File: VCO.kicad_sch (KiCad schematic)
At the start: 69 parts, among them K1 SW_SPST, K1-1 Conn_01x01, K1-2 Conn_01x01, K2 SW_SPST, K2-1 Conn_01x01, K2-2 Conn_01x01, K3 SW_SPST, K3-1 Conn_01x01, K3-2 Conn_01x01, P1-1-3 Conn_01x01, P1-2 Conn_01x01, P2 100k, P2-3 Conn_01x01, P3 100k, P3-1 Conn_01x01, P3-3 Conn_01x01, P4 4k7, P4-2 Conn_01x01, P4-3 Conn_01x01, Q3 BC184, Q4 BC183B, Q5 BF244B, Q6 BC184, Q7 BF244B, Q8 BC184, U1 7413, U2 7490, U4 UA747

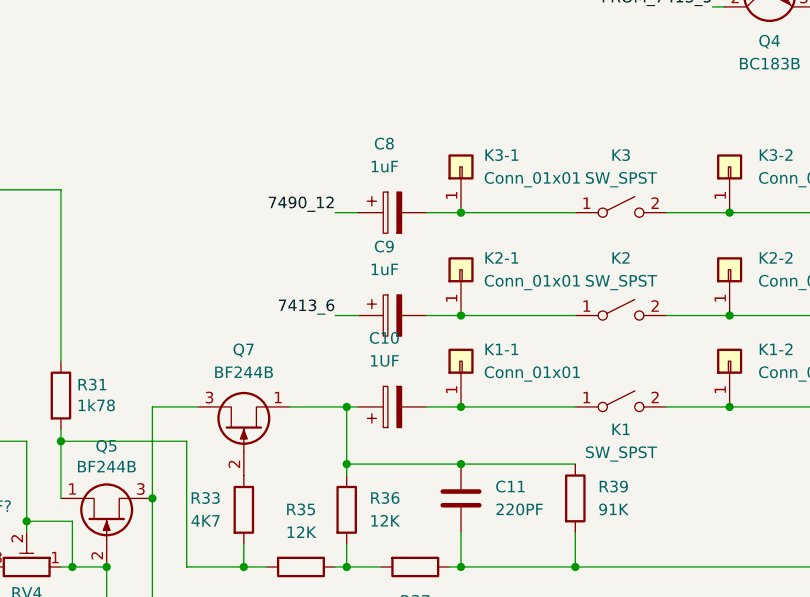
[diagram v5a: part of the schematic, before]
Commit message: Label connectors, update footprints
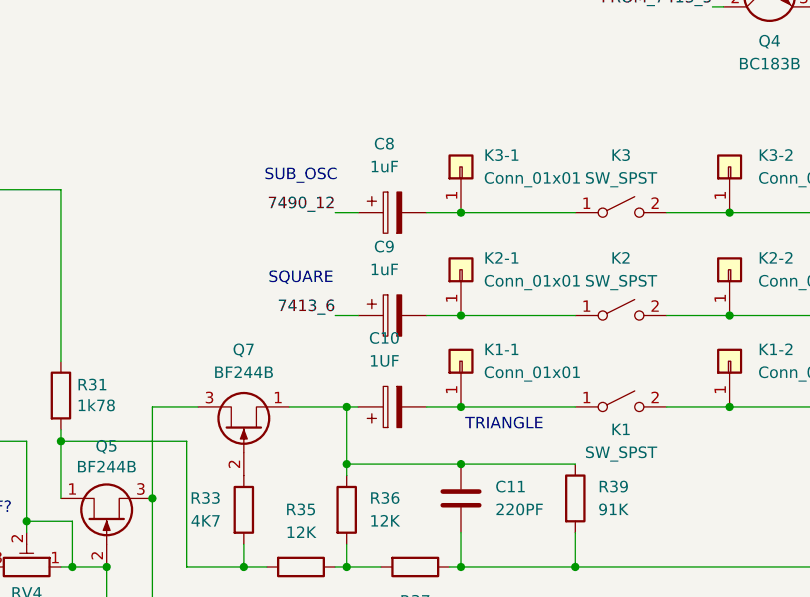
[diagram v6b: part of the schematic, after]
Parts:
- C10, C8: footprint (none) -> Capacitor_THT:CP_Radial_D6.3mm_P2.50mm
- C11, C6, C7: footprint (none) -> Capacitor_THT:C_Disc_D5.0mm_W2.5mm_P5.00mm
- C9: footprint (none) -> Capacitor_THT:CP_Radial_D8.0mm_P5.00mm
- D1, D2: footprint (none) -> Diode_THT:D_A-405_P10.16mm_Horizontal
- K1-1, K1-2, K2-1, K2-2, K3-1, K3-2, P1-1-3, P1-2, P2-3, P3-1, P3-3, P4-2, P4-3: footprint (none) -> Connector_PinHeader_2.54mm:PinHeader_1x01_P2.54mm_Vertical
- R18, R19, R20, R21, R23, R24, R25, R26, R27, R28, R29, R30, R31, R32, R33, R34, R35, R36, R37, R38, R39, R40, R41, R42, R43, R44, R45: footprint (none) -> Resistor_THT:R_Axial_DIN0207_L6.3mm_D2.5mm_P15.24mm_Horizontal
- RV16, RV17, RV22, RV4, RV46: footprint (none) -> Potentiometer_THT:Potentiometer_Bourns_3296W_Vertical
- U1, U2, U4: footprint (none) -> Package_DIP:DIP-14_W7.62mm_Socket_LongPads
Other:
- note added: "SQUARE"
- note added: "SUB_OSC"
- note added: "TRIANGLE"
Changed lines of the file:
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@@
 	(generator_version "9.0")
 	(paper "A4")
+	(text "SUB_OSC"
+		(exclude_from_sim no)
+		(at 184.15 58.166 0)
+		(effects
+			(font
+				(size 1.27 1.27)
+			)
+		)
+	)
+	(text "SQUARE"
+		(exclude_from_sim no)
+		(at 184.15 69.596 0)
+		(effects
+			(font
+				(size 1.27 1.27)
+			)
+		)
+	)
+	(text "TRIANGLE"
+		(exclude_from_sim no)
+		(at 206.756 85.852 0)
+		(effects
+			(font
+				(size 1.27 1.27)
+			)
+		)
+	)
 	(text "WTF?"
 		(exclude_from_sim no)
@@
 			)
 		)
-		(property "Footprint" ""
+		(property "Footprint" "Potentiometer_THT:Potentiometer_Bourns_3296W_Vertical"
 			(at 214.63 26.67 0)
 			(effects
@@
 			)
 		)
-		(property "Footprint" ""
+		(property "Footprint" "Resistor_THT:R_Axial_DIN0207_L6.3mm_D2.5mm_P15.24mm_Horizontal"
 			(at 229.87 28.702 90)
 			(effects
@@
 			)
 		)
-		(property "Footprint" ""
+		(property "Footprint" "Resistor_THT:R_Axial_DIN0207_L6.3mm_D2.5mm_P15.24mm_Horizontal"
 			(at 246.38 24.892 90)
 			(effects
@@
 			)
 		)
-		(property "Footprint" ""
+		(property "Footprint" "Package_DIP:DIP-14_W7.62mm_Socket_LongPads"
 			(at 58.42 115.57 0)
 			(effects
@@
 			)
 		)
-		(property "Footprint" ""
+		(property "Footprint" "Resistor_THT:R_Axial_DIN0207_L6.3mm_D2.5mm_P15.24mm_Horizontal"
 			(at 18.542 107.95 90)
 			(effects
@@
 			)
 		)
-		(property "Footprint" ""
+		(property "Footprint" "Resistor_THT:R_Axial_DIN0207_L6.3mm_D2.5mm_P15.24mm_Horizontal"
 			(at 22.098 162.56 90)
 			(effects
@@
 			)
 		)
-		(property "Footprint" ""
+		(property "Footprint" "Package_DIP:DIP-14_W7.62mm_Socket_LongPads"
 			(at 58.42 72.39 0)
 			(effects
@@
 			)
 		)
-		(property "Footprint" ""
+		(property "Footprint" "Capacitor_THT:CP_Radial_D6.3mm_P2.50mm"
 			(at 198.12 63.1952 0)
 			(effects
@@
 			)
 		)
-		(property "Footprint" ""
+		(property "Footprint" "Resistor_THT:R_Axial_DIN0207_L6.3mm_D2.5mm_P15.24mm_Horizontal"
 			(at 248.92 60.452 90)
 			(effects
@@
 			)
 		)
-		(property "Footprint" ""
+		(property "Footprint" "Resistor_THT:R_Axial_DIN0207_L6.3mm_D2.5mm_P15.24mm_Horizontal"
 			(at 248.92 71.882 90)
 			(effects
@@
 			)
 		)
-		(property "Footprint" ""
+		(property "Footprint" "Resistor_THT:R_Axial_DIN0207_L6.3mm_D2.5mm_P15.24mm_Horizontal"
 			(at 248.92 82.042 90)
 			(effects
@@
 			)
 		)
-		(property "Footprint" ""
+		(property "Footprint" "Resistor_THT:R_Axial_DIN0207_L6.3mm_D2.5mm_P15.24mm_Horizontal"
 			(at 141.732 76.2 90)
 			(effects
@@
 			)
 		)
-		(property "Footprint" ""
+		(property "Footprint" "Capacitor_THT:C_Disc_D5.0mm_W2.5mm_P5.00mm"
 			(at 127.3048 90.805 0)
 			(effects
@@
 			)
 		)
-		(property "Footprint" ""
+		(property "Footprint" "Potentiometer_THT:Potentiometer_Bourns_3296W_Vertical"
 			(at 153.67 101.6 0)
 			(effects
@@
 			)
 		)
-		(property "Footprint" ""
+		(property "Footprint" "Potentiometer_THT:Potentiometer_Bourns_3296W_Vertical"
 			(at 120.65 63.5 0)
 			(effects
@@
 			)
 		)
-		(property "Footprint" ""
+		(property "Footprint" "Diode_THT:D_A-405_P10.16mm_Horizontal"
 			(at 128.27 64.77 0)
 			(effects
@@
 			)
 		)
-		(property "Footprint" ""
+		(property "Footprint" "Diode_THT:D_A-405_P10.16mm_Horizontal"
 			(at 128.27 53.34 0)
 			(effects
@@
 			)
 		)
-		(property "Footprint" ""
+		(property "Footprint" "Resistor_THT:R_Axial_DIN0207_L6.3mm_D2.5mm_P15.24mm_Horizontal"
 			(at 155.702 82.55 90)
 			(effects
@@
 			)
 		)
-		(property "Footprint" ""
+		(property "Footprint" "Capacitor_THT:CP_Radial_D8.0mm_P5.00mm"
 			(at 198.12 74.6252 0)
 			(effects
@@
 			)
 		)
-		(property "Footprint" ""
+		(property "Footprint" "Capacitor_THT:CP_Radial_D6.3mm_P2.50mm"
 			(at 198.12 82.8548 0)
 			(effects
@@
 			)
 		)
-		(property "Footprint" ""
+		(property "Footprint" "Resistor_THT:R_Axial_DIN0207_L6.3mm_D2.5mm_P15.24mm_Horizontal"
 			(at 176.022 95.25 90)
 			(effects
@@
 			)
 		)
-		(property "Footprint" ""
+		(property "Footprint" "Resistor_THT:R_Axial_DIN0207_L6.3mm_D2.5mm_P15.24mm_Horizontal"
 			(at 184.15 99.822 90)
 			(effects
@@
 			)
 		)
-		(property "Footprint" ""
+		(property "Footprint" "Resistor_THT:R_Axial_DIN0207_L6.3mm_D2.5mm_P15.24mm_Horizontal"
 			(at 196.85 99.822 90)
 			(effects
@@
 			)
 		)
-		(property "Footprint" ""
+		(property "Footprint" "Resistor_THT:R_Axial_DIN0207_L6.3mm_D2.5mm_P15.24mm_Horizontal"
 			(at 187.452 95.25 90)
 			(effects
@@
 			)
 		)
-		(property "Footprint" ""
+		(property "Footprint" "Capacitor_THT:C_Disc_D5.0mm_W2.5mm_P5.00mm"
 			(at 202.8952 97.79 0)
 			(effects
@@
 			)
 		)
-		(property "Footprint" ""
+		(property "Footprint" "Resistor_THT:R_Axial_DIN0207_L6.3mm_D2.5mm_P15.24mm_Horizontal"
 			(at 212.852 93.98 90)
 			(effects
@@
 			)
 		)
-		(property "Footprint" ""
+		(property "Footprint" "Resistor_THT:R_Axial_DIN0207_L6.3mm_D2.5mm_P15.24mm_Horizontal"
 			(at 116.84 123.952 90)
 			(effects
@@
 			)
 		)
-		(property "Footprint" ""
+		(property "Footprint" "Potentiometer_THT:Potentiometer_Bourns_3296W_Vertical"
 			(at 106.68 152.4 0)
 			(effects
@@
 			)
 		)
-		(property "Footprint" ""
+		(property "Footprint" "Resistor_THT:R_Axial_DIN0207_L6.3mm_D2.5mm_P15.24mm_Horizontal"
 			(at 116.84 150.622 90)
 			(effects
@@
 			)
 		)
-		(property "Footprint" ""
+		(property "Footprint" "Resistor_THT:R_Axial_DIN0207_L6.3mm_D2.5mm_P15.24mm_Horizontal"
 			(at 137.922 115.57 90)
 			(effects
@@
 			)
 		)
-		(property "Footprint" ""
+		(property "Footprint" "Resistor_THT:R_Axial_DIN0207_L6.3mm_D2.5mm_P15.24mm_Horizontal"
 			(at 128.27 123.952 90)
 			(effects
@@
 			)
 		)
-		(property "Footprint" ""
+		(property "Footprint" "Resistor_THT:R_Axial_DIN0207_L6.3mm_D2.5mm_P15.24mm_Horizontal"
 			(at 146.812 125.73 90)
 			(effects
@@
 			)
 		)
-		(property "Footprint" ""
+		(property "Footprint" "Resistor_THT:R_Axial_DIN0207_L6.3mm_D2.5mm_P15.24mm_Horizontal"
 			(at 168.402 113.665 90)
 			(effects
@@
 			)
 		)
-		(property "Footprint" ""
+		(property "Footprint" "Package_DIP:DIP-14_W7.62mm_Socket_LongPads"
 			(at 162.56 146.05 0)
 			(effects
@@
 			)
 		)
-		(property "Footprint" ""
+		(property "Footprint" "Package_DIP:DIP-14_W7.62mm_Socket_LongPads"
 			(at 217.17 148.59 0)
 			(effects
@@
 			)
 		)
-		(property "Footprint" ""
+		(property "Footprint" "Capacitor_THT:C_Disc_D5.0mm_W2.5mm_P5.00mm"
 			(at 161.29 159.7152 0)
 			(effects
@@
 			)
 		)
-		(property "Footprint" ""
+		(property "Footprint" "Resistor_THT:R_Axial_DIN0207_L6.3mm_D2.5mm_P15.24mm_Horizontal"
 			(at 176.022 143.51 90)
 			(effects
@@
 			)
 		)
-		(property "Footprint" ""
+		(property "Footprint" "Resistor_THT:R_Axial_DIN0207_L6.3mm_D2.5mm_P15.24mm_Horizontal"
 			(at 215.9 159.512 90)
 			(effects
@@
 			)
 		)
-		(property "Footprint" ""
+		(property "Footprint" "Resistor_THT:R_Axial_DIN0207_L6.3mm_D2.5mm_P15.24mm_Horizontal"
 			(at 203.962 142.24 90)
 			(effects
@@
 			)
 		)
-		(property "Footprint" ""
+		(property "Footprint" "Resistor_THT:R_Axial_DIN0207_L6.3mm_D2.5mm_P15.24mm_Horizontal"
 			(at 152.908 140.97 90)
 			(effects
@@
 			)
 		)
-		(property "Footprint" ""
+		(property "Footprint" "Resistor_THT:R_Axial_DIN0207_L6.3mm_D2.5mm_P15.24mm_Horizontal"
 			(at 200.66 150.622 90)
 			(effects
@@
 			)
 		)
-		(property "Footprint" ""
+		(property "Footprint" "Resistor_THT:R_Axial_DIN0207_L6.3mm_D2.5mm_P15.24mm_Horizontal"
 			(at 239.268 140.97 90)
 			(effects
@@
 			)
 		)
-		(property "Footprint" ""
+		(property "Footprint" "Potentiometer_THT:Potentiometer_Bourns_3296W_Vertical"
 			(at 237.49 148.59 0)
 			(effects
@@
 			)
 		)
-		(property "Footprint" ""
+		(property "Footprint" "Resistor_THT:R_Axial_DIN0207_L6.3mm_D2.5mm_P15.24mm_Horizontal"
 			(at 138.43 172.212 90)
 			(effects
@@
 			)
 		)
-		(property "Footprint" ""
+		(property "Footprint" "Connector_PinHeader_2.54mm:PinHeader_1x01_P2.54mm_Vertical"
 			(at 111.125 130.81 0)
 			(effects
@@
 			)
 		)
-		(property "Footprint" ""
+		(property "Footprint" "Connector_PinHeader_2.54mm:PinHeader_1x01_P2.54mm_Vertical"
 			(at 201.93 57.15 0)
 			(effects
@@
 			)
 		)
-		(property "Footprint" ""
+		(property "Footprint" "Connector_PinHeader_2.54mm:PinHeader_1x01_P2.54mm_Vertical"
 			(at 201.93 78.74 0)
 			(effects
@@
 			)
 		)
-		(property "Footprint" ""
+		(property "Footprint" "Connector_PinHeader_2.54mm:PinHeader_1x01_P2.54mm_Vertical"
 			(at 231.775 57.15 0)
 			(effects
@@
 			)
 		)
-		(property "Footprint" ""
+		(property "Footprint" "Connector_PinHeader_2.54mm:PinHeader_1x01_P2.54mm_Vertical"
 			(at 231.775 78.74 0)
 			(effects
@@
 			)
 		)
-		(property "Footprint" ""
+		(property "Footprint" "Connector_PinHeader_2.54mm:PinHeader_1x01_P2.54mm_Vertical"
 			(at 134.62 120.65 0)
 			(effects
@@
 			)
 		)
-		(property "Footprint" ""
+		(property "Footprint" "Connector_PinHeader_2.54mm:PinHeader_1x01_P2.54mm_Vertical"
 			(at 201.93 68.58 0)
 			(effects
@@
 			)
 		)
-		(property "Footprint" ""
+		(property "Footprint" "Connector_PinHeader_2.54mm:PinHeader_1x01_P2.54mm_Vertical"
 			(at 231.775 68.58 0)
 			(effects
@@
 			)
 		)
-		(property "Footprint" ""
+		(property "Footprint" "Connector_PinHeader_2.54mm:PinHeader_1x01_P2.54mm_Vertical"
 			(at 198.12 31.75 0)
 			(effects
@@
 			)
 		)
-		(property "Footprint" ""
+		(property "Footprint" "Connector_PinHeader_2.54mm:PinHeader_1x01_P2.54mm_Vertical"
 			(at 191.135 159.385 0)
 			(effects
@@
 			)
 		)
-		(property "Footprint" ""
+		(property "Footprint" "Connector_PinHeader_2.54mm:PinHeader_1x01_P2.54mm_Vertical"
 			(at 190.5 147.32 0)
 			(effects
@@
 			)
 		)
-		(property "Footprint" ""
+		(property "Footprint" "Connector_PinHeader_2.54mm:PinHeader_1x01_P2.54mm_Vertical"
 			(at 209.55 31.75 0)
 			(effects
@@
 			)
 		)
-		(property "Footprint" ""
+		(property "Footprint" "Connector_PinHeader_2.54mm:PinHeader_1x01_P2.54mm_Vertical"
 			(at 134.62 130.81 0)
 			(effects
@@
 			)
 		)
-		(property "Footprint" ""
+		(property "Footprint" "Package_DIP:DIP-14_W7.62mm_Socket_LongPads"
 			(at 58.42 170.18 0)
 			(effects
